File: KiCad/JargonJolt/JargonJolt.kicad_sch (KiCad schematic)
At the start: 0 parts

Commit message: worked on schematic
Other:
- sheet MCU ports: added HSPI_CS1, HSPI_CS2, HSPI_MOSI, HSPI_SCLK; removed none
- sheet Memory ports: added CS1, CS2, MISO, MOSI, SCLK; removed VSPI_CS1, VSPI_CS2, VSPI_MISO, VSPI_MOSI, VSPI_SCLK
- sheet User Interface ports: added BUSY1, BUSY2, CS1, CS2, DC1, DC2, MOSI, RST, SCLK; removed none
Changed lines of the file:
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@@
 (kicad_sch (version 20230121) (generator eeschema)
   (paper "A4")
-  (wire (pts (xy 107.061 86.106) (xy 111.76 86.106))
+  (wire (pts (xy 135.255 107.442) (xy 153.67 107.442))
     (stroke (width 0) (type default))
   )
-  (wire (pts (xy 83.312 117.348) (xy 111.76 117.348))
+  (wire (pts (xy 81.28 101.6) (xy 99.695 101.6))
     (stroke (width 0) (type default))
   )
-  (wire (pts (xy 83.185 114.681) (xy 109.347 114.681))
+  (wire (pts (xy 135.255 93.98) (xy 153.67 93.98))
     (stroke (width 0) (type default))
   )
-  (wire (pts (xy 83.185 112.395) (xy 107.061 112.395))
+  (wire (pts (xy 81.28 94.615) (xy 99.695 94.615))
     (stroke (width 0) (type default))
   )
-  (wire (pts (xy 147.32 90.678) (xy 165.608 90.678))
+  (wire (pts (xy 135.255 102.743) (xy 153.67 102.743))
     (stroke (width 0) (type default))
   )
-  (wire (pts (xy 109.347 114.681) (xy 109.347 88.011))
+  (wire (pts (xy 81.28 97.155) (xy 99.695 97.155))
     (stroke (width 0) (type default))
   )
-  (wire (pts (xy 147.32 85.979) (xy 165.608 85.979))
+  (wire (pts (xy 135.255 92.075) (xy 153.67 92.075))
     (stroke (width 0) (type default))
   )
-  (wire (pts (xy 107.061 112.395) (xy 107.061 86.106))
+  (wire (pts (xy 81.28 92.71) (xy 99.695 92.71))
     (stroke (width 0) (type default))
   )
-  (wire (pts (xy 104.902 83.566) (xy 111.76 83.566))
+  (wire (pts (xy 135.255 95.885) (xy 153.67 95.885))
     (stroke (width 0) (type default))
   )
-  (wire (pts (xy 147.32 88.392) (xy 165.608 88.392))
+  (wire (pts (xy 81.28 99.06) (xy 99.695 99.06))
     (stroke (width 0) (type default))
   )
-  (wire (pts (xy 83.058 110.363) (xy 104.902 110.363))
+  (wire (pts (xy 135.255 105.156) (xy 153.67 105.156))
     (stroke (width 0) (type default))
   )
-  (wire (pts (xy 109.347 88.011) (xy 111.76 88.011))
+  (wire (pts (xy 135.255 88.265) (xy 153.67 88.265))
     (stroke (width 0) (type default))
   )
-  (wire (pts (xy 111.76 117.348) (xy 111.76 90.17))
-    (stroke (width 0) (type default))
-  )
-  (wire (pts (xy 104.902 110.363) (xy 104.902 83.566))
-    (stroke (width 0) (type default))
-  )
-  (sheet (at 165.608 79.756) (size 23.495 11.938) (fields_autoplaced)
+  (sheet (at 153.67 84.074) (size 23.495 37.211) (fields_autoplaced)
     (stroke (width 0.1524) (type solid))
     (fill (color 200 255 102 1.0000))
-    (property "Sheetname" "User Interface" (at 165.608 79.0444 0)
+    (property "Sheetname" "User Interface" (at 153.67 83.3624 0)
       (effects (font (size 1.27 1.27)) (justify left bottom))
     )
-    (property "Sheetfile" "ui.kicad_sch" (at 165.608 92.2786 0)
+    (property "Sheetfile" "ui.kicad_sch" (at 153.67 121.8696 0)
       (effects (font (size 1.27 1.27)) (justify left top))
     )
-    (pin "BUTTON1" input (at 165.608 85.979 180)
+    (pin "BUTTON1" output (at 153.67 102.743 180)
       (effects (font (size 1.27 1.27)) (justify left))
     )
-    (pin "BUTTON2" input (at 165.608 88.392 180)
+    (pin "BUTTON2" output (at 153.67 105.156 180)
       (effects (font (size 1.27 1.27)) (justify left))
     )
-    (pin "BUTTON3" input (at 165.608 90.678 180)
+    (pin "BUTTON3" output (at 153.67 107.442 180)
+      (effects (font (size 1.27 1.27)) (justify left))
+    )
+    (pin "SCLK" input (at 153.67 88.265 180)
+      (effects (font (size 1.27 1.27)) (justify left))
+    )
+    (pin "MOSI" input (at 153.67 92.075 180)
+      (effects (font (size 1.27 1.27)) (justify left))
+    )
+    (pin "CS1" input (at 153.67 93.98 180)
+      (effects (font (size 1.27 1.27)) (justify left))
+    )
+    (pin "CS2" input (at 153.67 95.885 180)
+      (effects (font (size 1.27 1.27)) (justify left))
+    )
+    (pin "BUSY1" output (at 153.67 111.125 180)
+      (effects (font (size 1.27 1.27)) (justify left))
+    )
+    (pin "DC2" output (at 153.67 116.84 180)
+      (effects (font (size 1.27 1.27)) (justify left))
+    )
+    (pin "BUSY2" output (at 153.67 113.03 180)
+      (effects (font (size 1.27 1.27)) (justify left))
+    )
+    (pin "DC1" output (at 153.67 114.935 180)
+      (effects (font (size 1.27 1.27)) (justify left))
+    )
+    (pin "RST" output (at 153.67 118.745 180)
       (effects (font (size 1.27 1.27)) (justify left))
     )
@@
     )
   )
-  (sheet (at 63.5 106.68) (size 19.685 17.78) (fields_autoplaced)
+  (sheet (at 61.595 90.805) (size 19.685 17.78) (fields_autoplaced)
     (stroke (width 0.1524) (type solid))
     (fill (color 113 64 255 1.0000))
-    (property "Sheetname" "Memory" (at 63.5 105.9684 0)
+    (property "Sheetname" "Memory" (at 61.595 90.0934 0)
       (effects (font (size 1.27 1.27)) (justify left bottom))
     )
-    (property "Sheetfile" "memory.kicad_sch" (at 63.5 125.0446 0)
+    (property "Sheetfile" "memory.kicad_sch" (at 61.595 109.1696 0)
       (effects (font (size 1.27 1.27)) (justify left top))
     )
-    (pin "VSPI_CS1" input (at 83.185 110.49 0)
+    (pin "MISO" input (at 81.28 99.06 0)
       (effects (font (size 1.27 1.27)) (justify right))
     )
-    (pin "VSPI_MOSI" input (at 83.185 112.522 0)
+    (pin "CS1" input (at 81.28 94.615 0)
       (effects (font (size 1.27 1.27)) (justify right))
     )
-    (pin "VSPI_MISO" input (at 83.185 114.808 0)
+    (pin "CS2" input (at 81.28 92.71 0)
       (effects (font (size 1.27 1.27)) (justify right))
     )
-    (pin "VSPI_CS2" input (at 83.185 108.077 0)
+    (pin "MOSI" input (at 81.28 97.155 0)
       (effects (font (size 1.27 1.27)) (justify right))
     )
-    (pin "VSPI_SCLK" input (at 83.185 117.348 0)
+    (pin "SCLK" input (at 81.28 101.6 0)
       (effects (font (size 1.27 1.27)) (justify right))
     )
@@
     )
   )
-  (sheet (at 118.745 114.3) (size 23.495 7.62) (fields_autoplaced)
+  (sheet (at 189.23 97.155) (size 23.495 7.62) (fields_autoplaced)
     (stroke (width 0.1524) (type solid))
     (fill (color 255 94 97 1.0000))
-    (property "Sheetname" "Power" (at 118.745 113.5884 0)
+    (property "Sheetname" "Power" (at 189.23 96.4434 0)
       (effects (font (size 1.27 1.27)) (justify left bottom))
     )
-    (property "Sheetfile" "power.kicad_sch" (at 118.745 122.5046 0)
+    (property "Sheetfile" "power.kicad_sch" (at 189.23 105.3596 0)
       (effects (font (size 1.27 1.27)) (justify left top))
     )
@@
     )
   )
-  (sheet (at 111.76 67.31) (size 35.56 24.765) (fields_autoplaced)
+  (sheet (at 99.695 84.074) (size 35.56 24.765) (fields_autoplaced)
     (stroke (width 0.1524) (type solid))
     (fill (color 91 138 255 1.0000))
-    (property "Sheetname" "MCU" (at 111.76 66.5984 0)
+    (property "Sheetname" "MCU" (at 99.695 83.3624 0)
       (effects (font (size 1.27 1.27)) (justify left bottom))
     )
-    (property "Sheetfile" "mcu.kicad_sch" (at 111.76 92.6596 0)
+    (property "Sheetfile" "mcu.kicad_sch" (at 99.695 109.4236 0)
       (effects (font (size 1.27 1.27)) (justify left top))
     )
-    (pin "BUTTON1" input (at 147.32 85.979 0)
+    (pin "BUTTON1" input (at 135.255 102.743 0)
       (effects (font (size 1.27 1.27)) (justify right))
     )
-    (pin "BUTTON2" input (at 147.32 88.392 0)
+    (pin "BUTTON2" input (at 135.255 105.156 0)
       (effects (font (size 1.27 1.27)) (justify right))
     )
-    (pin "VSPI_MOSI" input (at 111.76 86.106 180)
+    (pin "VSPI_MOSI" output (at 99.695 97.155 180)
       (effects (font (size 1.27 1.27)) (justify left))
     )
-    (pin "VSPI_SCLK" input (at 111.76 90.17 180)
+    (pin "VSPI_SCLK" output (at 99.695 101.6 180)
       (effects (font (size 1.27 1.27)) (justify left))
     )
-    (pin "VSPI_MISO" input (at 111.76 88.011 180)
+    (pin "VSPI_MISO" output (at 99.695 99.06 180)
       (effects (font (size 1.27 1.27)) (justify left))
     )
-    (pin "VSPI_CS1" input (at 111.76 83.566 180)
+    (pin "VSPI_CS1" output (at 99.695 94.615 180)
       (effects (font (size 1.27 1.27)) (justify left))
     )
-    (pin "VSPI_CS2" input (at 111.76 81.28 180)
+    (pin "VSPI_CS2" output (at 99.695 92.71 180)
       (effects (font (size 1.27 1.27)) (justify left))
     )
-    (pin "BUTTON3" input (at 147.32 90.678 0)
+    (pin "BUTTON3" input (at 135.255 107.442 0)
       (effects (font (size 1.27 1.27)) (justify right))
     )
+    (pin "HSPI_SCLK" output (at 135.255 88.265 0)
+      (effects (font (size 1.27 1.27)) (justify right))
+    )
+    (pin "HSPI_MOSI" output (at 135.255 92.075 0)
+      (effects (font (size 1.27 1.27)) (justify right))
+    )
+    (pin "HSPI_CS1" output (at 135.255 93.98 0)
+      (effects (font (size 1.27 1.27)) (justify right))
+    )
+    (pin "HSPI_CS2" output (at 135.255 95.885 0)
+      (effects (font (size 1.27 1.27)) (justify right))
+    )

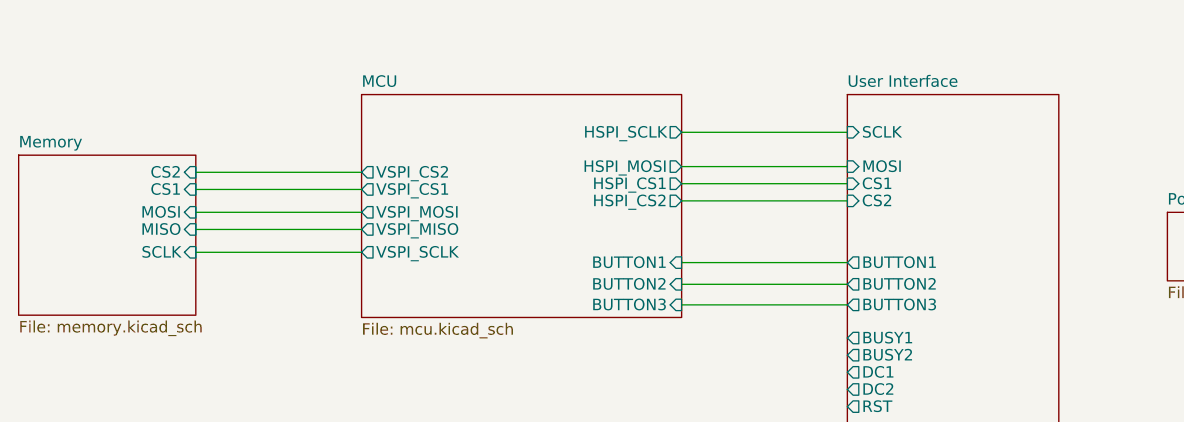
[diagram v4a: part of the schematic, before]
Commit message: added i2s schematic
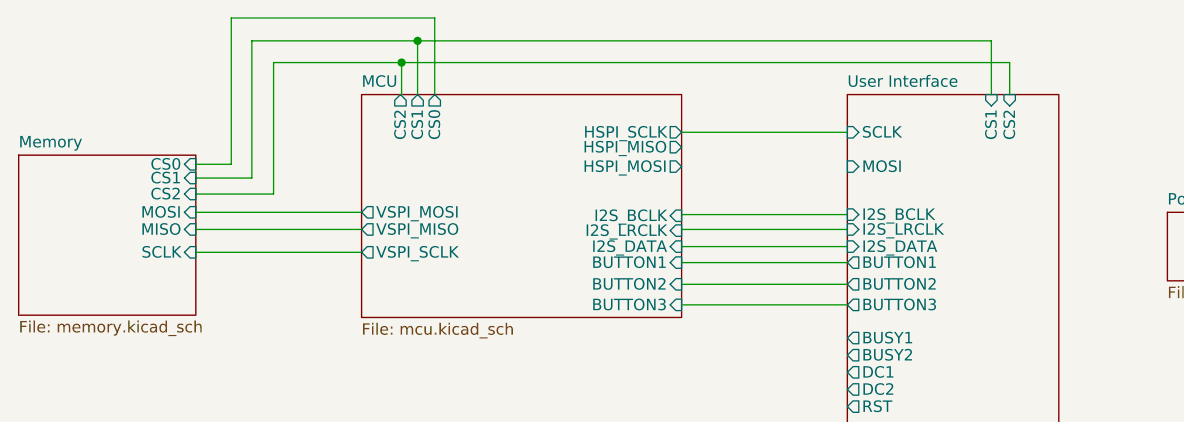
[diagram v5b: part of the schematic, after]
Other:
- sheet MCU ports: added CS0, CS1, CS2, HSPI_MISO, I2S_BCLK, I2S_DATA, I2S_LRCLK; removed HSPI_CS1, HSPI_CS2, VSPI_CS1, VSPI_CS2
- sheet Memory ports: added CS0; removed none
- sheet User Interface ports: added I2S_BCLK, I2S_DATA, I2S_LRCLK; removed none
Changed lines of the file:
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@@
 (kicad_sch (version 20230121) (generator eeschema)
   (paper "A4")
+  (junction (at 104.14 80.518) (diameter 0) (color 0 0 0 0)
+  )
+  (junction (at 105.918 78.105) (diameter 0) (color 0 0 0 0)
+  )
+  (wire (pts (xy 135.255 97.409) (xy 153.67 97.409))
+    (stroke (width 0) (type default))
+  )
+  (wire (pts (xy 104.14 84.074) (xy 104.013 84.074))
+    (stroke (width 0) (type default))
+  )
+  (wire (pts (xy 85.217 91.821) (xy 81.28 91.821))
+    (stroke (width 0) (type default))
+  )
   (wire (pts (xy 135.255 107.442) (xy 153.67 107.442))
     (stroke (width 0) (type default))
   )
+  (wire (pts (xy 89.916 80.518) (xy 89.916 95.123))
+    (stroke (width 0) (type default))
+  )
   (wire (pts (xy 81.28 101.6) (xy 99.695 101.6))
     (stroke (width 0) (type default))
   )
-  (wire (pts (xy 135.255 93.98) (xy 153.67 93.98))
-    (stroke (width 0) (type default))
-  )
-  (wire (pts (xy 81.28 94.615) (xy 99.695 94.615))
+  (wire (pts (xy 105.918 78.105) (xy 105.918 84.074))
+    (stroke (width 0) (type default))
+  )
+  (wire (pts (xy 104.14 80.518) (xy 104.14 84.074))
+    (stroke (width 0) (type default))
+  )
+  (wire (pts (xy 135.255 99.06) (xy 135.255 99.187))
+    (stroke (width 0) (type default))
+  )
+  (wire (pts (xy 87.503 93.345) (xy 81.28 93.345))
+    (stroke (width 0) (type default))
+  )
+  (wire (pts (xy 107.823 75.565) (xy 107.823 84.074))
+    (stroke (width 0) (type default))
+  )
+  (wire (pts (xy 81.28 97.155) (xy 99.695 97.155))
+    (stroke (width 0) (type default))
+  )
+  (wire (pts (xy 135.255 99.06) (xy 153.67 99.06))
+    (stroke (width 0) (type default))
+  )
+  (wire (pts (xy 104.14 80.518) (xy 89.916 80.518))
+    (stroke (width 0) (type default))
+  )
+  (wire (pts (xy 169.672 84.074) (xy 169.672 78.105))
+    (stroke (width 0) (type default))
+  )
+  (wire (pts (xy 89.916 95.123) (xy 81.28 95.123))
+    (stroke (width 0) (type default))
+  )
+  (wire (pts (xy 85.217 75.565) (xy 85.217 91.821))
+    (stroke (width 0) (type default))
+  )
+  (wire (pts (xy 169.672 78.105) (xy 105.918 78.105))
+    (stroke (width 0) (type default))
+  )
+  (wire (pts (xy 81.28 99.06) (xy 99.695 99.06))
+    (stroke (width 0) (type default))
+  )
+  (wire (pts (xy 135.255 100.965) (xy 153.67 100.965))
+    (stroke (width 0) (type default))
+  )
+  (wire (pts (xy 87.503 78.105) (xy 87.503 93.345))
+    (stroke (width 0) (type default))
+  )
+  (wire (pts (xy 105.918 78.105) (xy 87.503 78.105))
     (stroke (width 0) (type default))
   )
@@
     (stroke (width 0) (type default))
   )
-  (wire (pts (xy 81.28 97.155) (xy 99.695 97.155))
-    (stroke (width 0) (type default))
-  )
-  (wire (pts (xy 135.255 92.075) (xy 153.67 92.075))
-    (stroke (width 0) (type default))
-  )
-  (wire (pts (xy 81.28 92.71) (xy 99.695 92.71))
-    (stroke (width 0) (type default))
-  )
-  (wire (pts (xy 135.255 95.885) (xy 153.67 95.885))
-    (stroke (width 0) (type default))
-  )
-  (wire (pts (xy 81.28 99.06) (xy 99.695 99.06))
+  (wire (pts (xy 107.823 75.565) (xy 85.217 75.565))
+    (stroke (width 0) (type default))
+  )
+  (wire (pts (xy 171.704 84.074) (xy 171.704 80.518))
+    (stroke (width 0) (type default))
+  )
+  (wire (pts (xy 135.255 97.409) (xy 135.255 97.536))
     (stroke (width 0) (type default))
   )
@@
   )
   (wire (pts (xy 135.255 88.265) (xy 153.67 88.265))
+    (stroke (width 0) (type default))
+  )
+  (wire (pts (xy 171.704 80.518) (xy 104.14 80.518))
     (stroke (width 0) (type default))
   )
@@
       (effects (font (size 1.27 1.27)) (justify left))
     )
-    (pin "CS1" input (at 153.67 93.98 180)
-      (effects (font (size 1.27 1.27)) (justify left))
-    )
-    (pin "CS2" input (at 153.67 95.885 180)
-      (effects (font (size 1.27 1.27)) (justify left))
+    (pin "CS1" input (at 169.672 84.074 90)
+      (effects (font (size 1.27 1.27)) (justify right))
+    )
+    (pin "CS2" input (at 171.704 84.074 90)
+      (effects (font (size 1.27 1.27)) (justify right))
     )
     (pin "BUSY1" output (at 153.67 111.125 180)
@@
     )
     (pin "RST" output (at 153.67 118.745 180)
+      (effects (font (size 1.27 1.27)) (justify left))
+    )
+    (pin "I2S_LRCLK" input (at 153.67 99.06 180)
+      (effects (font (size 1.27 1.27)) (justify left))
+    )
+    (pin "I2S_BCLK" input (at 153.67 97.409 180)
+      (effects (font (size 1.27 1.27)) (justify left))
+    )
+    (pin "I2S_DATA" input (at 153.67 100.965 180)
       (effects (font (size 1.27 1.27)) (justify left))
     )
@@
       (effects (font (size 1.27 1.27)) (justify right))
     )
-    (pin "CS1" input (at 81.28 94.615 0)
-      (effects (font (size 1.27 1.27)) (justify right))
-    )
-    (pin "CS2" input (at 81.28 92.71 0)
+    (pin "CS1" input (at 81.28 93.345 0)
+      (effects (font (size 1.27 1.27)) (justify right))
+    )
+    (pin "CS2" input (at 81.28 95.123 0)
       (effects (font (size 1.27 1.27)) (justify right))
     )
@@
     )
     (pin "SCLK" input (at 81.28 101.6 0)
+      (effects (font (size 1.27 1.27)) (justify right))
+    )
+    (pin "CS0" input (at 81.28 91.821 0)
       (effects (font (size 1.27 1.27)) (justify right))
     )
@@
       (effects (font (size 1.27 1.27)) (justify left))
     )
-    (pin "VSPI_CS1" output (at 99.695 94.615 180)
-      (effects (font (size 1.27 1.27)) (justify left))
-    )
-    (pin "VSPI_CS2" output (at 99.695 92.71 180)
-      (effects (font (size 1.27 1.27)) (justify left))
-    )
     (pin "BUTTON3" input (at 135.255 107.442 0)
       (effects (font (size 1.27 1.27)) (justify right))
@@
       (effects (font (size 1.27 1.27)) (justify right))
     )
-    (pin "HSPI_CS1" output (at 135.255 93.98 0)
-      (effects (font (size 1.27 1.27)) (justify right))
-    )
-    (pin "HSPI_CS2" output (at 135.255 95.885 0)
-      (effects (font (size 1.27 1.27)) (justify right))
-    )
+    (pin "HSPI_MISO" output (at 135.255 89.916 0)
+      (effects (font (size 1.27 1.27)) (justify right))
+    )
+    (pin "I2S_BCLK" input (at 135.255 97.536 0)
+      (effects (font (size 1.27 1.27)) (justify right))
+    )
+    (pin "I2S_LRCLK" input (at 135.255 99.187 0)
+      (effects (font (size 1.27 1.27)) (justify right))
+    )
+    (pin "I2S_DATA" input (at 135.255 100.965 0)
+      (effects (font (size 1.27 1.27)) (justify right))
+    )
+    (pin "CS2" output (at 104.013 84.074 90)
+      (effects (font (size 1.27 1.27)) (justify right))
+    )
+    (pin "CS1" output (at 105.918 84.074 90)
+      (effects (font (size 1.27 1.27)) (justify right))
+    )
+    (pin "CS0" output (at 107.823 84.074 90)
+      (effects (font (size 1.27 1.27)) (justify right))
+    )
